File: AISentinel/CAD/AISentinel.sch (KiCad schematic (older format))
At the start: 29 parts

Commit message: Diagram vompleted
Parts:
- removed Q?: BC547, symbol NPN
- removed R?: 10k, symbol R
- added D3: 1N4148, symbol DIODE
- added K1: RELAY, symbol RELAY-V23092
- added K2: HORN, symbol CONN_3
- added U2: 4N33, symbol PHDARL
- P2: renamed from P?; value BTN -> PUSH
- R1, R3: renamed from R?; value 10k -> 4k7
- SW1: renamed from SW?; value PUSHBUTTON -> SW
- gave numbers to parts that had none: 23
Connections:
- net labels added: A+, B-
- wire segments 89 -> 97
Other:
- moved on the sheet: C3, C4, D1, D2, IC1, P3, Q3, R1, R3, R6, R7, R8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

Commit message: Make it runon the prototype tiny24
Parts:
- removed K2: HORN, symbol CONN_3
- removed SW1: SW, symbol SW_PUSH
- removed U2: 4N33, symbol PHDARL
- added D4: 1N4148, symbol DIODE
- added P4: HORN, symbol CONN_2
- added R9: 68k, symbol R
- added U2: 4N26, symbol PHTRANS
- R1: value 4k7 -> 1k
- renumbered C4 to C3, C3 to C4, D3 to D1, D1 to D2, D2 to D3, P4 to P5, P5 to P6, P6 to P7, Q2 to Q1, Q3 to Q2, R3 to R2, R4 to R3, R6 to R4, R7 to R6, R8 to R7, R9 to R8
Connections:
- wire segments 97 -> 96
- no-connect marks 1 -> 2
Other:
- moved on the sheet: Q2, R2, R7, R8

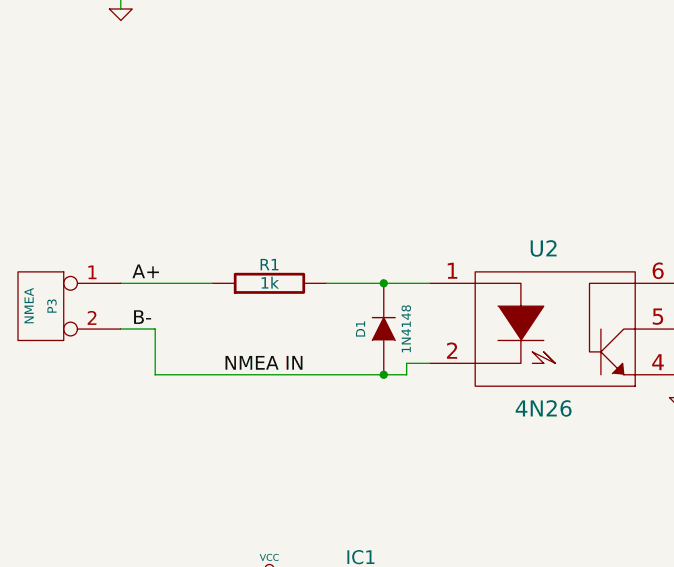
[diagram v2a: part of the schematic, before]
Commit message: AISentinel min activity LED blink duration Ack buttonpress disables sound as opposed to toggle Toggling was too confusing
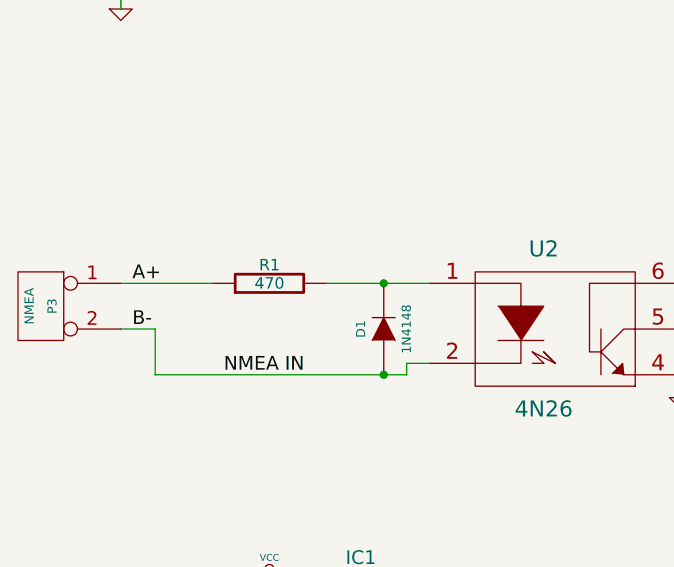
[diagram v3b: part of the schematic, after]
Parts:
- R1: value 1k -> 470
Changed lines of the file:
@@
-EESchema Schematic File Version 2  date 22-04-2012 23:03:51
+EESchema Schematic File Version 2  date 01-11-2012 14:08:30
 LIBS:power
 LIBS:device
@@
 Sheet 1 1
 Title "AISentinel"
-Date "22 apr 2012"
+Date "1 nov 2012"
 Rev "0"
 Comp "© MadsenSoft"
@@
 P 2800 4100
 F 0 "R1" V 2880 4100 50  0000 C CNN
-F 1 "1k" V 2800 4100 50  0000 C CNN
+F 1 "470" V 2800 4100 50  0000 C CNN
 	1    2800 4100
 	0    -1   -1   0
